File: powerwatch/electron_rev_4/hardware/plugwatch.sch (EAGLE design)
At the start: 121 parts, among them J1 DM3AT-SF-PEJM5, Q1 SI223DDS, Q2 MOSFET-NCHANNELSMD, U1 BGA725L6-ALT, U10 SIP32510, U12 SIP32510, U13 AB1815-T3, U14 MPU-9250, U16 MAX6746, U2 SAFFB1G56KB0F0A, U3 IRM-03-5V, U4 MAX-M8, U5 MAX9910, U6 SIP32510, U8 MAX9910, U9 SIP32510, X1 ABS07-32.768KHZ-7-T

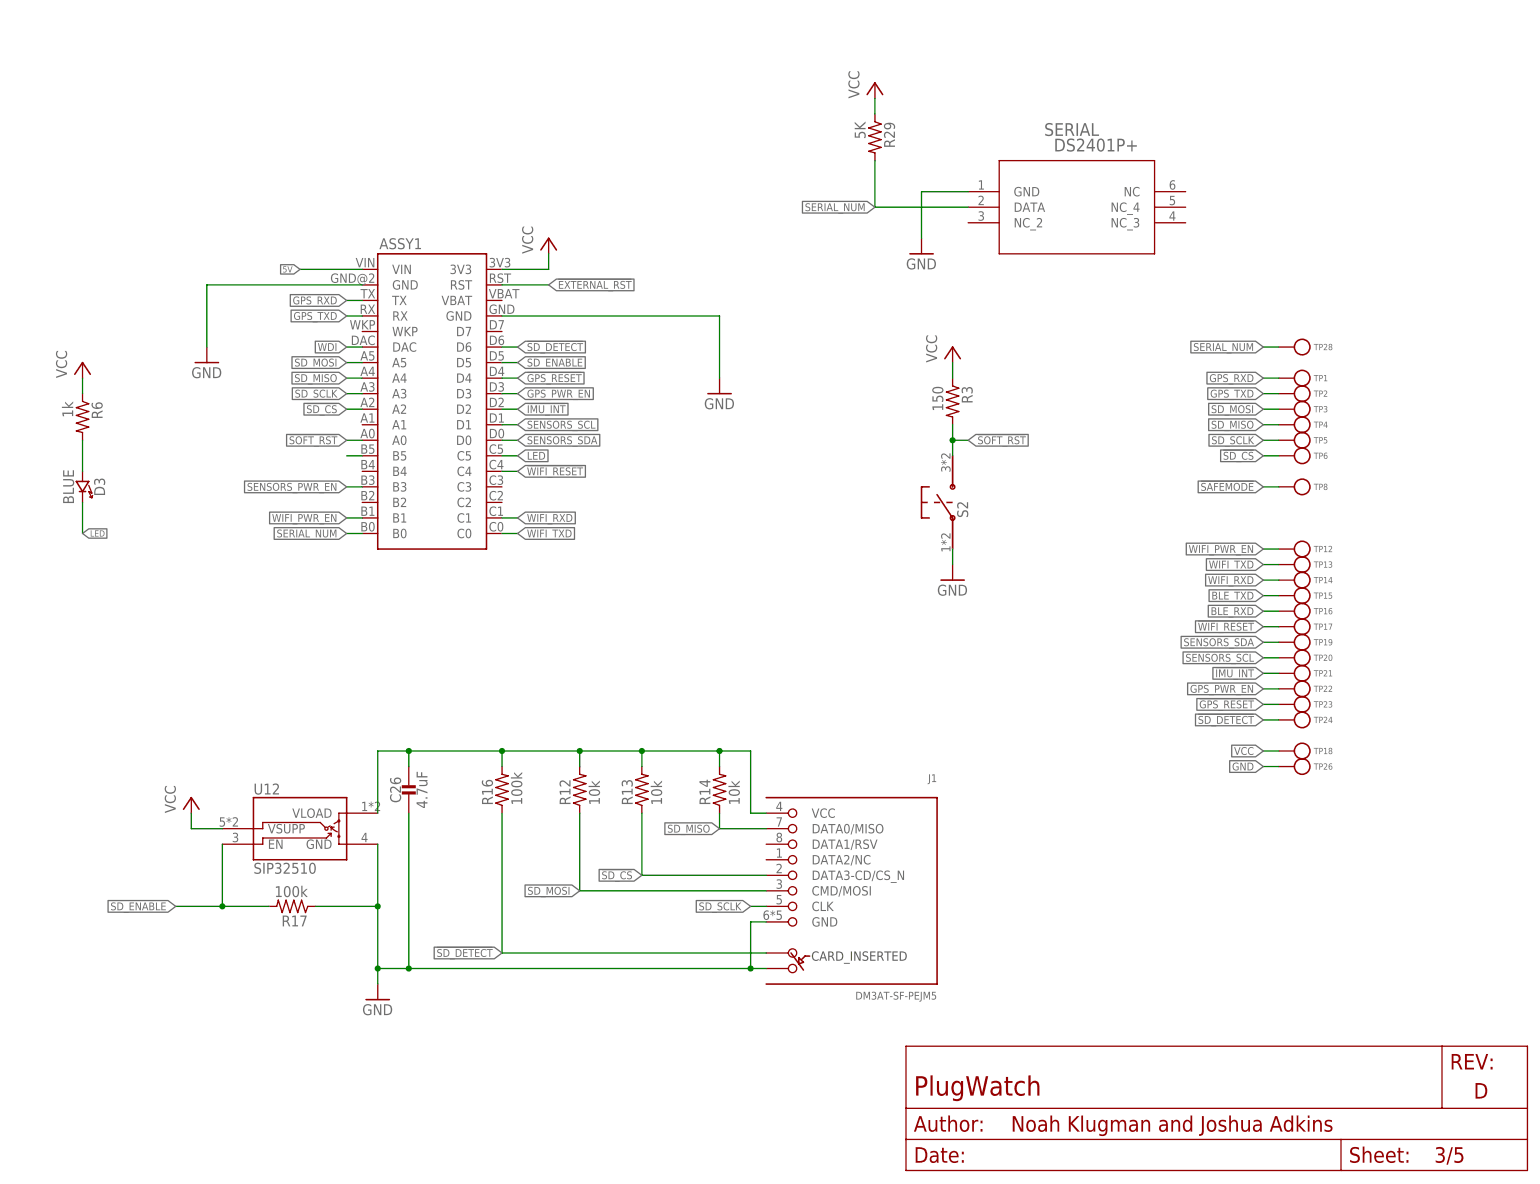
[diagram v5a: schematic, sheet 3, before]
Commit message: add mic, remove many old things, connect RTC, new Accel
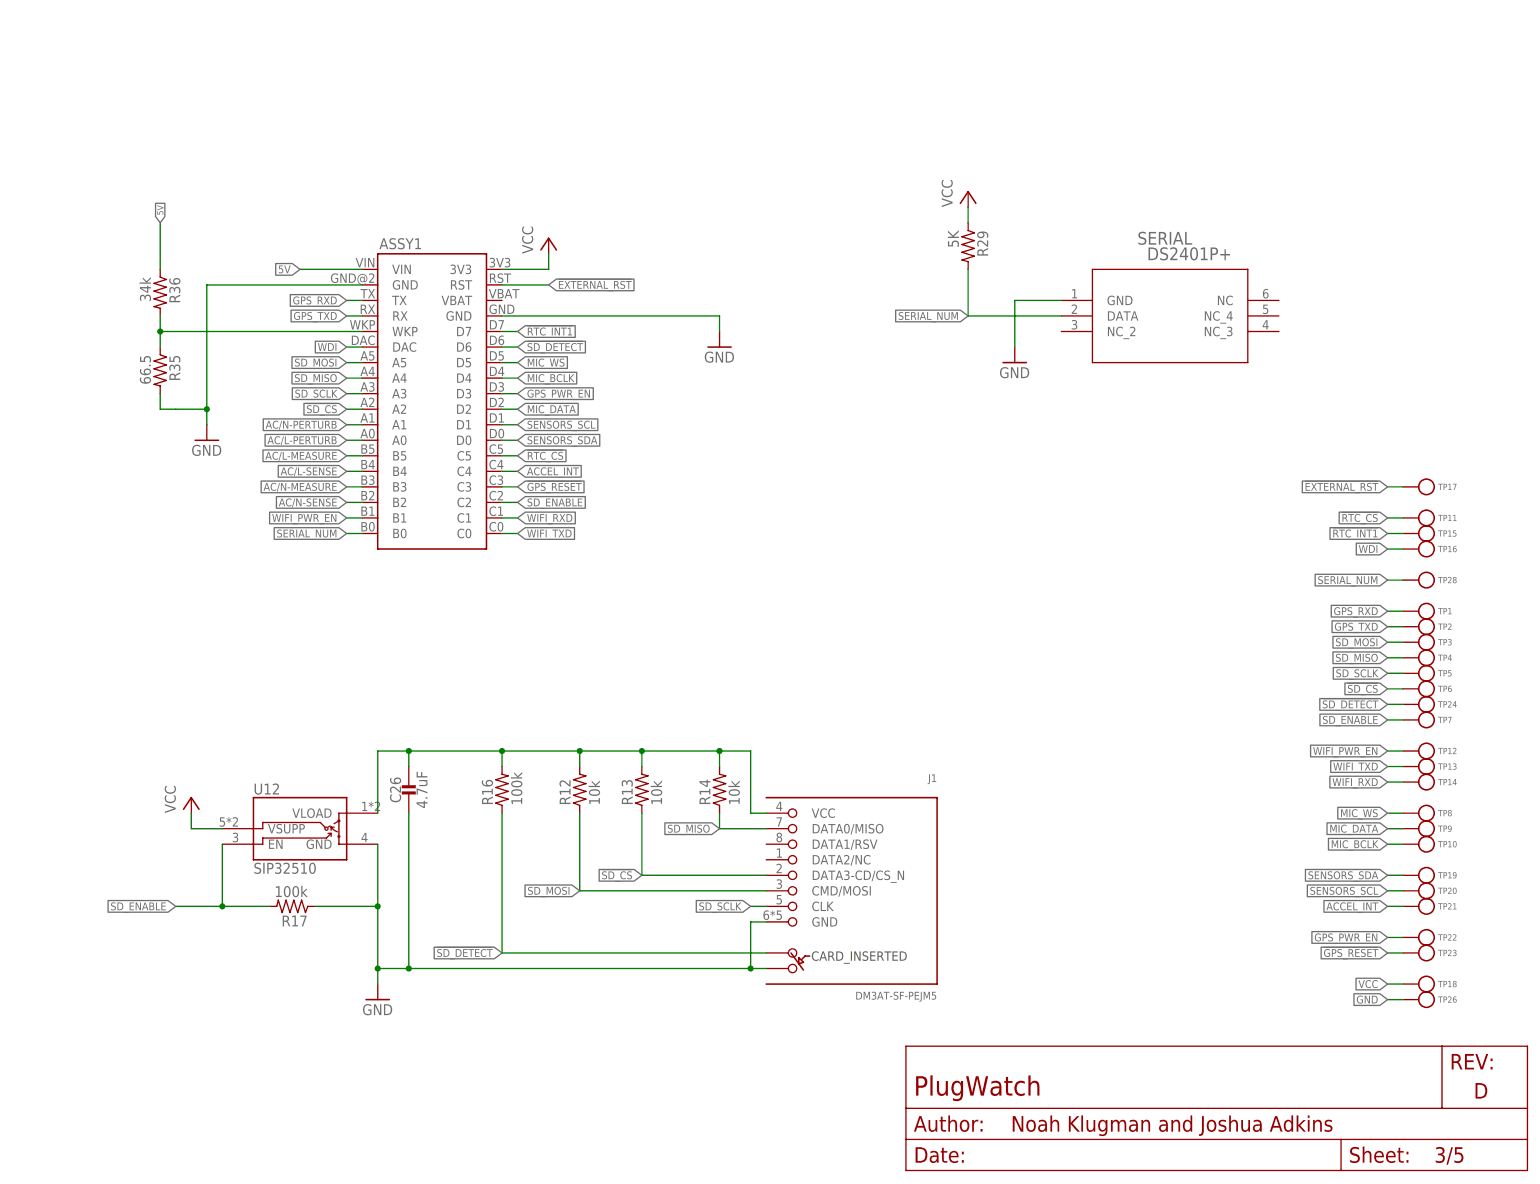
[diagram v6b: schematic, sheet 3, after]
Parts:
- removed C18: 100nF, passives:CAPACITOR0402_CAP
- removed D3: BLUE, leds:LED0603
- removed S2: PTS645SM43SMTR92, switches:PTS645SM43SMTR92
- removed U14: MPU-9250, chips:MPU-9250
- added R35: 66.5, passives:RESISTOR0402_RES
- added R36: 34k, passives:RESISTOR0402_RES
- added TP10, TP11, TP7, TP9: TEST_POINT_0.040IN, headers:TEST_POINT_0.040IN
- added U7: (no value), microphones:SPH0645LM4H-B
- C13: value 10nF -> 10uF
- C19: value 100nF -> 0.1uF
- R11: value 10k -> 68
- R26: value 100k -> 68; DESCRIPTION RES SMD 100K OHM 1% 1/16W 0402 -> RES SMD 10K OHM 1% 1/16W 0402; DIGIKEY 1276-3432-1-ND -> RMCF0402FT10K0CT-ND; MANUFACTURER Samsung -> Stackpole Electronics; MPN RC1005F104CS -> RMCF0402FT10K0
- R3: value 150 -> 68; DESCRIPTION RES SMD 150 OHM 1% 1/16W 0402 -> RES SMD 10K OHM 1% 1/16W 0402; DIGIKEY RMCF0402FT150RCT-ND -> RMCF0402FT10K0CT-ND; MPN RMCF0402FT150R -> RMCF0402FT10K0
- R6: value 1k -> 10k; DESCRIPTION RES SMD 1K OHM 1% 1/16W 0402 -> RES SMD 150 OHM 1% 1/16W 0402; DIGIKEY RMCF0402FT1K00CT-ND -> RMCF0402FT150RCT-ND; MPN RMCF0402FT1K00 -> RMCF0402FT150R
- U6: value SIP32510 -> LIS2DW12; device chips:SIP32510 -> chips:LIS2DW12
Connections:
- removed net !IMU_INT: ASSY1.D2, R11.1, TP21.TESTPOINT, U14.INT
- removed net !SAFEMODE: TP8.TESTPOINT
- removed net !SOFT_RST: ASSY1.A0, R3.2, S2.P$2
- removed net !WIFI_RESET: ASSY1.C4, ASSY2.!RST, TP17.TESTPOINT
- removed net BLE_PWR_EN: ASSY1.B5
- removed net BLE_RXD: TP16.TESTPOINT
- removed net BLE_TXD: TP15.TESTPOINT
- removed net LED: ASSY1.C5, D3.CATHODE
- removed net N$19: C18.1, U14.REGOUT
- removed net N$30: R26.1, U6.GND
- removed net SENSORS_PWR_EN: ASSY1.B3, R26.2, U6.EN
- removed net VCC_SENSORS: C13.1, C19.1, R10.2, R11.2, R9.2, U14.!CS, U14.VDD, U14.VDDIO, U6.VLOAD
- new net ACCEL_INT: ASSY1.C4, TP21.TESTPOINT, U6.INT1
- new net MIC_BCLK: ASSY1.D4, R11.2, TP10.TESTPOINT
- new net MIC_DATA: ASSY1.D2, R26.1, TP9.TESTPOINT
- new net MIC_WS: ASSY1.D5, R3.2, TP8.TESTPOINT
- new net N$10: ASSY1.WKP, R35.1, R36.2
- new net N$12: R11.1, U7.BCLK
- new net N$15: R26.2, U7.DATA
- net !EXTERNAL_RST: now also TP17.TESTPOINT
- net !GPS_RESET: now also ASSY1.C3; no longer ASSY1.D4
- net !RTC_CS: now also ASSY1.C5, R6.2, TP11.TESTPOINT
- net !RTC_INT1: now also ASSY1.D7, TP15.TESTPOINT
- net 5V: now also R36.1
- net AC/L-MEASURE: now also ASSY1.B5
- net AC/L-PERTURB: now also ASSY1.A0
- net AC/L-SENSE: now also ASSY1.B4
- net AC/N-MEASURE: now also ASSY1.B3
- net AC/N-PERTURB: now also ASSY1.A1
- net AC/N-SENSE: now also ASSY1.B2
- net GND: now also R35.2, U6.GND, U6.MISO/SA0, U7.GND; no longer C18.2, S2.P$1, U14.AD0/MISO, U14.FSYNC, U14.GND
- net N$14: now also ASSY2.!RST
- net N$3: now also R3.1, U7.WS; no longer D3.ANODE, R6.2
- net SD_ENABLE: now also ASSY1.C2, TP7.TESTPOINT; no longer ASSY1.D5
- net SENSORS_SCL: now also R9.1, U6.SCL/SPC; no longer R10.1, U14.SCLK
- net SENSORS_SDA: now also R10.1, U6.MOSI/SDA; no longer R9.1, U14.SDA/MOSI
- net VCC: now also C13.1, C19.1, R10.2, R9.2, U6.CS, U6.VCC, U6.VDD_IO, U7.SELECT, U7.VDD; no longer R3.1, U6.VSUPP
- net WDI: now also TP16.TESTPOINT
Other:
- note added: "Accelerometer"
- note added: "Divide 5v down to 3.3v. Wkp will wake up particle from deep sleep on rising edge."
- note added: "I2C Address: 0x18"
- note added: "Pull CS high to enable I2C mode. Pull SA0 low to zero last address bit."
- note removed: "Accelerometer/Magnetometer"
- note removed: "I2C Address: 0x68"
- note removed: "Note: GPIO choices are arbitrary"
- moved on the sheet: C13, C19, C3, R10, R11, R26, R29, R9, SERIAL, TP1, TP12, TP13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

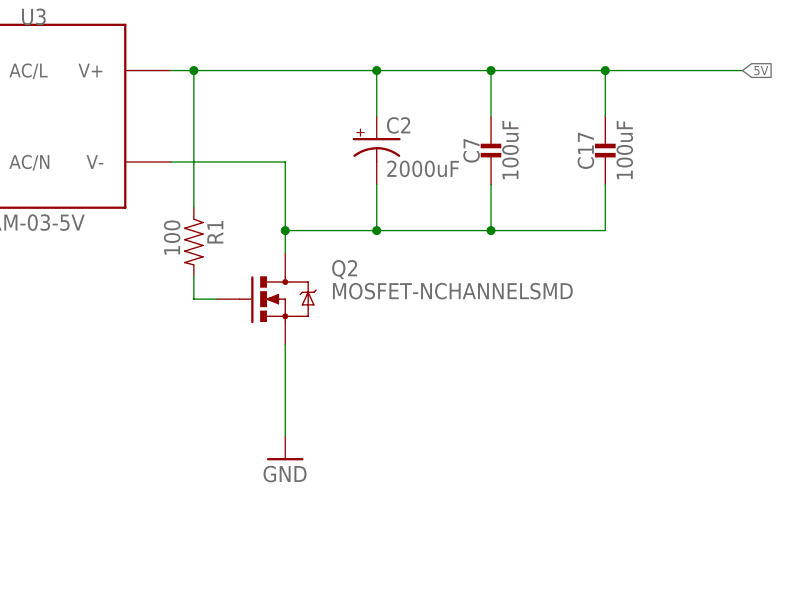
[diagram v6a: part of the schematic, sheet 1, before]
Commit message: switch the gnd float mosfet?
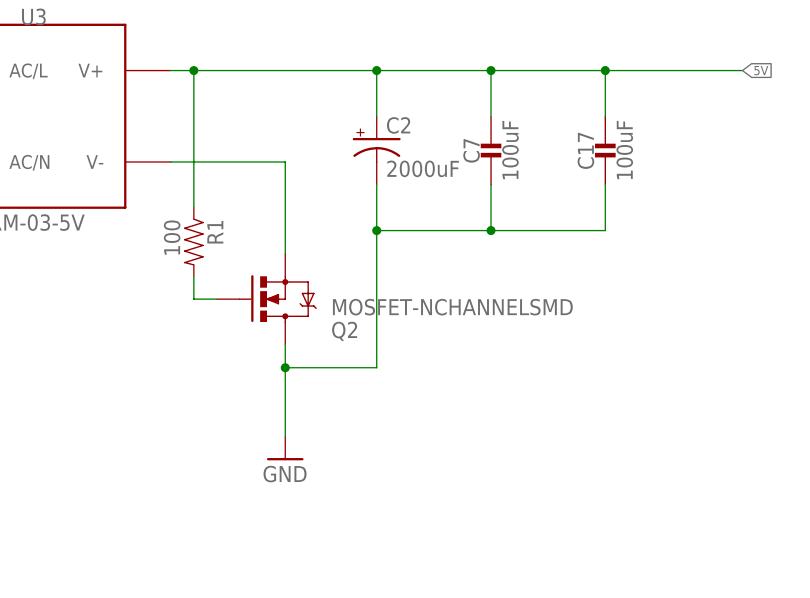
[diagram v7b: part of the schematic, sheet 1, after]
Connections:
- removed net N$9: C17.2, C2.-, C7.2, Q2.D, U3.V-
- new net N$8: Q2.S, U3.V-
- net GND: now also C17.2, C2.-, C7.2, Q2.D; no longer Q2.S
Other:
- note added: "Note that source is connected to V-...I am a bit unsure if this correct for the perturb circuit."
- moved on the sheet: Q2
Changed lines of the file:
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@@
 <text x="66.04" y="137.16" size="1.016" layer="98" align="bottom-center">We use a seperate AC Measure pin so that we can more directly sense the perturbation by the digital output.
 The full-scale voltage sensing circuit (below) could also be used, but would only sense &lt;1% of its dynamic range.</text>
+<text x="154.94" y="147.32" size="1.27" layer="98" align="bottom-center">Note that source is connected to V-...I am a bit unsure if this correct for the perturb circuit.</text>
 </plain>
 <instances>
@@
 <instance part="C7" gate="G$1" x="165.1" y="162.56"/>
 <instance part="C17" gate="G$1" x="177.8" y="162.56"/>
-<instance part="Q2" gate="G$1" x="142.24" y="144.78"/>
+<instance part="Q2" gate="G$1" x="142.24" y="144.78" rot="MR180"/>
 <instance part="R1" gate="G$1" x="132.08" y="149.86" rot="R270">
 <attribute name="DIGIKEY" x="132.08" y="149.86" size="1.27" layer="96" rot="R270" display="off"/>
@@
 </segment>
 </net>
-<net name="N$9" class="0">
-<segment>
-<pinref part="U3" gate="G$1" pin="V-"/>
-<wire x1="129.54" y1="160.02" x2="142.24" y2="160.02" width="0.1524" layer="91"/>
-<wire x1="142.24" y1="160.02" x2="142.24" y2="152.4" width="0.1524" layer="91"/>
+<net name="GND" class="0">
+<segment>
+<pinref part="SUPPLY1" gate="1" pin="GND"/>
+<wire x1="142.24" y1="129.54" x2="142.24" y2="137.16" width="0.1524" layer="91"/>
 <wire x1="152.4" y1="157.48" x2="152.4" y2="152.4" width="0.1524" layer="91"/>
-<wire x1="152.4" y1="152.4" x2="142.24" y2="152.4" width="0.1524" layer="91"/>
 <wire x1="165.1" y1="157.48" x2="165.1" y2="152.4" width="0.1524" layer="91"/>
 <wire x1="165.1" y1="152.4" x2="152.4" y2="152.4" width="0.1524" layer="91"/>
-<junction x="152.4" y="152.4"/>
 <wire x1="177.8" y1="157.48" x2="177.8" y2="152.4" width="0.1524" layer="91"/>
 <wire x1="177.8" y1="152.4" x2="165.1" y2="152.4" width="0.1524" layer="91"/>
@@
 <pinref part="C7" gate="G$1" pin="2"/>
 <pinref part="C17" gate="G$1" pin="2"/>
+<wire x1="152.4" y1="152.4" x2="152.4" y2="137.16" width="0.1524" layer="91"/>
+<junction x="152.4" y="152.4"/>
+<wire x1="152.4" y1="137.16" x2="142.24" y2="137.16" width="0.1524" layer="91"/>
 <pinref part="Q2" gate="G$1" pin="D"/>
-<wire x1="142.24" y1="149.86" x2="142.24" y2="152.4" width="0.1524" layer="91"/>
-<junction x="142.24" y="152.4"/>
-</segment>
-</net>
-<net name="GND" class="0">
-<segment>
-<pinref part="SUPPLY1" gate="1" pin="GND"/>
-<pinref part="Q2" gate="G$1" pin="S"/>
-<wire x1="142.24" y1="129.54" x2="142.24" y2="139.7" width="0.1524" layer="91"/>
+<wire x1="142.24" y1="139.7" x2="142.24" y2="137.16" width="0.1524" layer="91"/>
+<junction x="142.24" y="137.16"/>
 </segment>
 <segment>
@@
 <net name="N$32" class="0">
 <segment>
-<pinref part="Q2" gate="G$1" pin="G"/>
-<wire x1="134.62" y1="144.78" x2="132.08" y2="144.78" width="0.1524" layer="91"/>
 <pinref part="R1" gate="G$1" pin="2"/>
 <wire x1="132.08" y1="144.78" x2="132.08" y2="147.32" width="0.1524" layer="91"/>
+<pinref part="Q2" gate="G$1" pin="G"/>
+<wire x1="132.08" y1="144.78" x2="134.62" y2="144.78" width="0.1524" layer="91"/>
 </segment>
 </net>
@@
 </segment>
 </net>
+<net name="N$8" class="0">
+<segment>
+<pinref part="U3" gate="G$1" pin="V-"/>
+<wire x1="129.54" y1="160.02" x2="142.24" y2="160.02" width="0.1524" layer="91"/>
+<pinref part="Q2" gate="G$1" pin="S"/>
+<wire x1="142.24" y1="149.86" x2="142.24" y2="160.02" width="0.1524" layer="91"/>
+</segment>
+</net>
